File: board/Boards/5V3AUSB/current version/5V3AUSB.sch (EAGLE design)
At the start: 11 parts

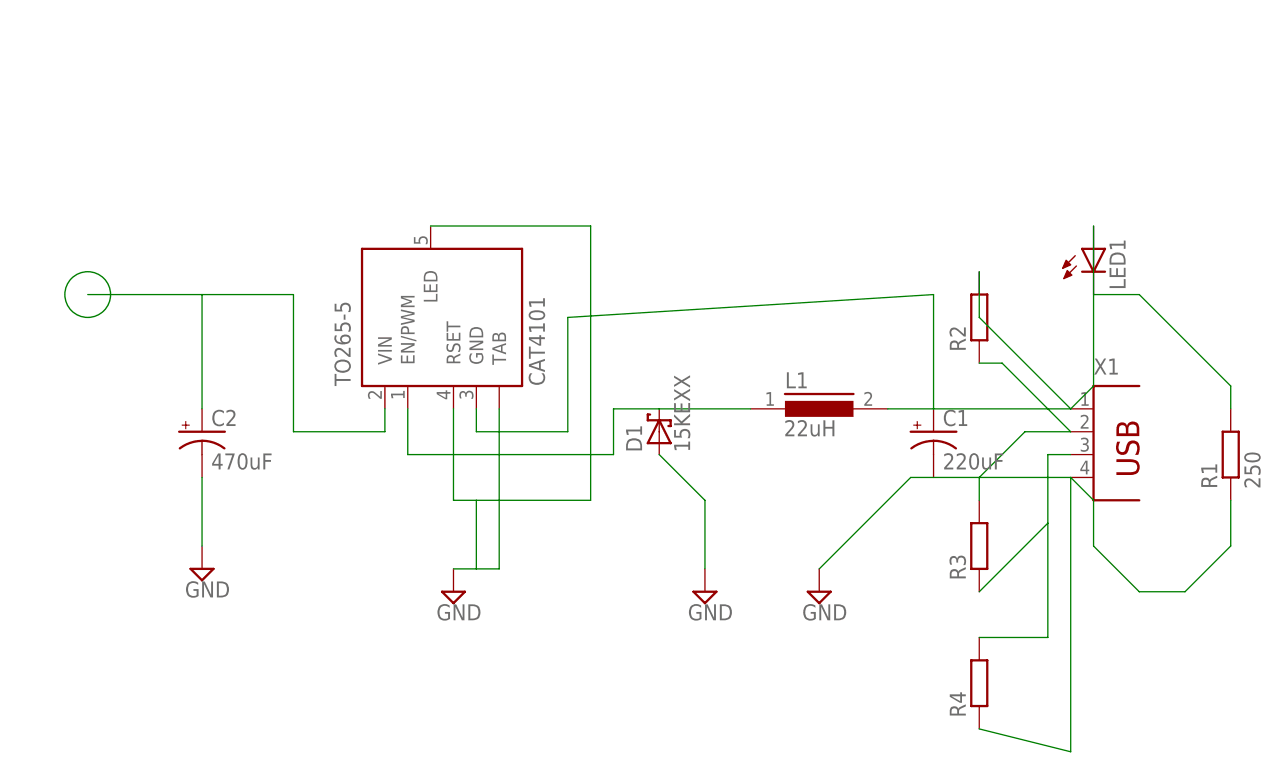
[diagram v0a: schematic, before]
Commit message: updates to the 5V3A board
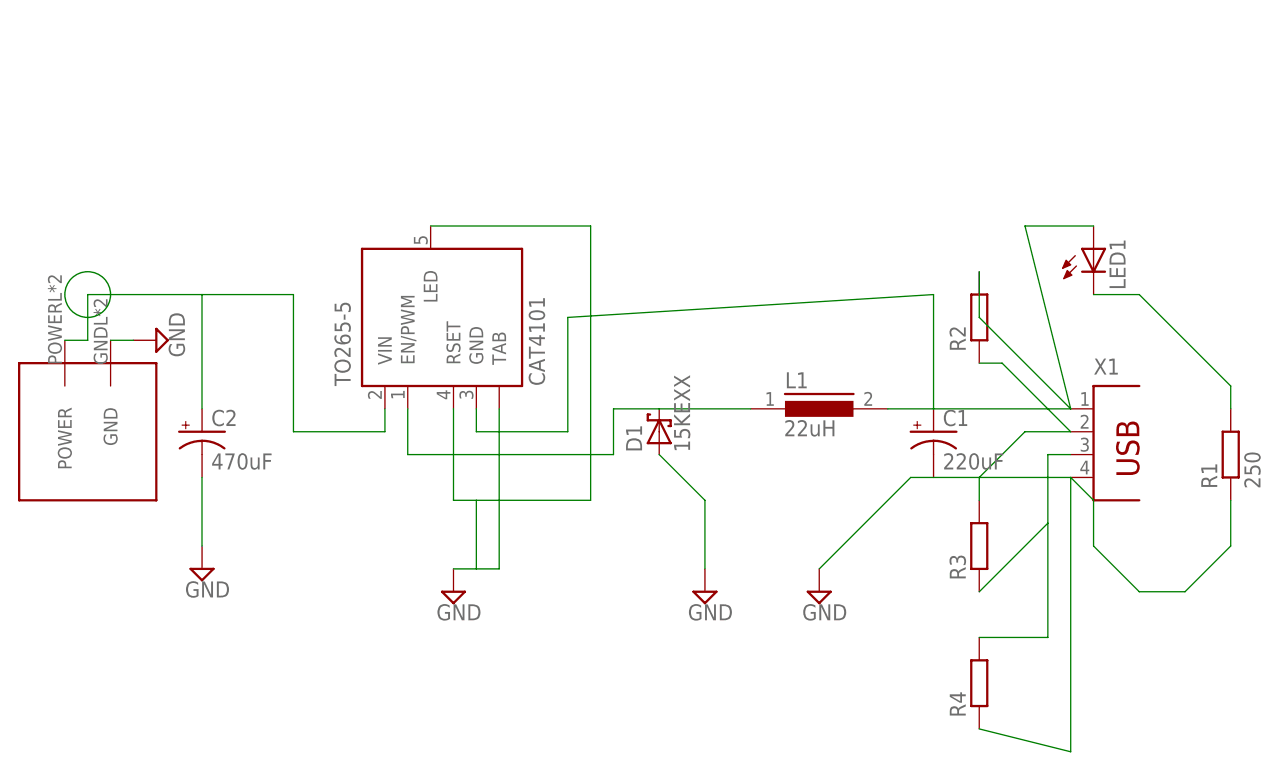
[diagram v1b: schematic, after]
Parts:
- added U$1: 2X2-MOLEX, Molex:2X2-MOLEX
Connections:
- net GND: now also U$1.GND
- net N$1: now also U$1.POWER
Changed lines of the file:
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@@
 <part name="LED1" library="led" deviceset="LED" device="CHIPLED_1206"/>
 <part name="R1" library="resistor" deviceset="R-EU_" device="R1206" value="250"/>
+<part name="U$1" library="Molex" deviceset="2X2-MOLEX" device=""/>
+<part name="SUPPLY5" library="supply2" deviceset="GND" device=""/>
 </parts>
 <sheets>
@@
 <instance part="LED1" gate="G$1" x="137.16" y="121.92"/>
 <instance part="R1" gate="G$1" x="152.4" y="99.06" rot="R90"/>
+<instance part="U$1" gate="G$1" x="25.4" y="99.06"/>
+<instance part="SUPPLY5" gate="GND" x="33.02" y="111.76" rot="R90"/>
 </instances>
 <busses>
@@
 <pinref part="TO265-5" gate="G$1" pin="VIN"/>
 <wire x1="58.42" y1="101.6" x2="58.42" y2="104.14" width="0.1524" layer="91"/>
+<pinref part="U$1" gate="G$1" pin="POWER"/>
+<wire x1="22.86" y1="111.76" x2="25.4" y2="111.76" width="0.1524" layer="91"/>
+<wire x1="25.4" y1="111.76" x2="25.4" y2="116.84" width="0.1524" layer="91"/>
 </segment>
 </net>
@@
 <wire x1="68.58" y1="86.36" x2="71.12" y2="86.36" width="0.1524" layer="91"/>
 </segment>
+<segment>
+<pinref part="U$1" gate="G$1" pin="GND"/>
+<pinref part="SUPPLY5" gate="GND" pin="GND"/>
+<wire x1="27.94" y1="111.76" x2="30.48" y2="111.76" width="0.1524" layer="91"/>
+</segment>
 </net>
 <net name="N$2" class="0">
@@
 <wire x1="119.38" y1="104.14" x2="134.62" y2="104.14" width="0.1524" layer="91"/>
 <pinref part="LED1" gate="G$1" pin="A"/>
-<wire x1="137.16" y1="124.46" x2="137.16" y2="106.68" width="0.1524" layer="91"/>
-<wire x1="137.16" y1="106.68" x2="134.62" y2="104.14" width="0.1524" layer="91"/>
+<wire x1="137.16" y1="124.46" x2="129.54" y2="124.46" width="0.1524" layer="91"/>
+<wire x1="129.54" y1="124.46" x2="134.62" y2="104.14" width="0.1524" layer="91"/>
 </segment>
 </net>

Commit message: getting ready to add pads out +5V
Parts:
- added TP1, TP2: TP2P2-38-20, testpad:TP2P2-38-20
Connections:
- net GND: now also TP1B.TP, TP2B.TP
- net N$3: now also TP1A.TP, TP2A.TP
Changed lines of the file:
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@@
 <part name="U$1" library="Molex" deviceset="2X2-MOLEX" device=""/>
 <part name="SUPPLY5" library="supply2" deviceset="GND" device=""/>
+<part name="TP1" library="testpad" deviceset="TP2" device="P2-38-20"/>
+<part name="TP2" library="testpad" deviceset="TP2" device="P2-38-20"/>
+<part name="SUPPLY6" library="supply2" deviceset="GND" device=""/>
 </parts>
 <sheets>
@@
 <instance part="U$1" gate="G$1" x="25.4" y="99.06"/>
 <instance part="SUPPLY5" gate="GND" x="33.02" y="111.76" rot="R90"/>
+<instance part="TP1" gate="A" x="86.36" y="127"/>
+<instance part="TP1" gate="B" x="93.98" y="127"/>
+<instance part="TP2" gate="A" x="101.6" y="127"/>
+<instance part="TP2" gate="B" x="109.22" y="127"/>
+<instance part="SUPPLY6" gate="GND" x="116.84" y="121.92"/>
 </instances>
 <busses>
@@
 <wire x1="27.94" y1="111.76" x2="30.48" y2="111.76" width="0.1524" layer="91"/>
 </segment>
+<segment>
+<pinref part="TP1" gate="B" pin="TP"/>
+<wire x1="93.98" y1="124.46" x2="96.52" y2="124.46" width="0.1524" layer="91"/>
+<wire x1="96.52" y1="124.46" x2="96.52" y2="129.54" width="0.1524" layer="91"/>
+<pinref part="SUPPLY6" gate="GND" pin="GND"/>
+<wire x1="96.52" y1="129.54" x2="116.84" y2="129.54" width="0.1524" layer="91"/>
+<wire x1="116.84" y1="129.54" x2="116.84" y2="124.46" width="0.1524" layer="91"/>
+<pinref part="TP2" gate="B" pin="TP"/>
+<wire x1="109.22" y1="124.46" x2="111.76" y2="124.46" width="0.1524" layer="91"/>
+<wire x1="111.76" y1="124.46" x2="111.76" y2="127" width="0.1524" layer="91"/>
+<wire x1="111.76" y1="127" x2="114.3" y2="127" width="0.1524" layer="91"/>
+<wire x1="114.3" y1="127" x2="114.3" y2="124.46" width="0.1524" layer="91"/>
+<wire x1="114.3" y1="124.46" x2="116.84" y2="124.46" width="0.1524" layer="91"/>
+</segment>
 </net>
 <net name="N$2" class="0">
@@
 <wire x1="137.16" y1="124.46" x2="129.54" y2="124.46" width="0.1524" layer="91"/>
 <wire x1="129.54" y1="124.46" x2="134.62" y2="104.14" width="0.1524" layer="91"/>
+<pinref part="TP1" gate="A" pin="TP"/>
+<wire x1="86.36" y1="124.46" x2="119.38" y2="104.14" width="0.1524" layer="91"/>
+<pinref part="TP2" gate="A" pin="TP"/>
+<wire x1="101.6" y1="124.46" x2="119.38" y2="104.14" width="0.1524" layer="91"/>
 </segment>
 </net>

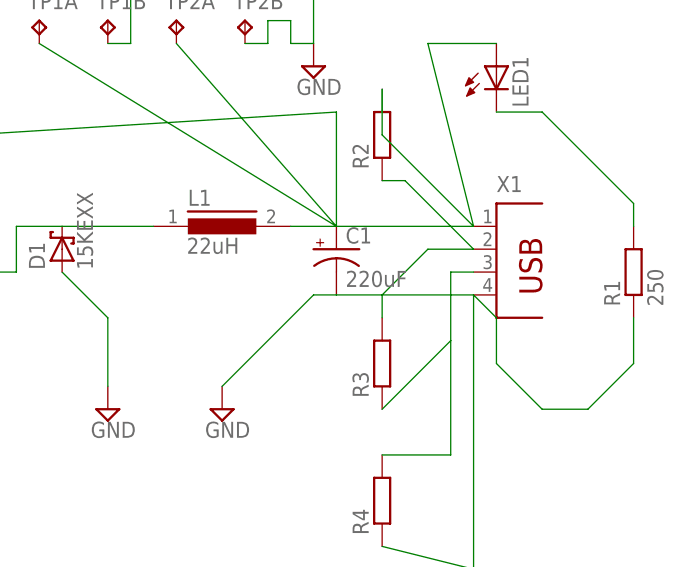
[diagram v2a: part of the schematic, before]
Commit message: board placement is looking good. going to verify schematic now
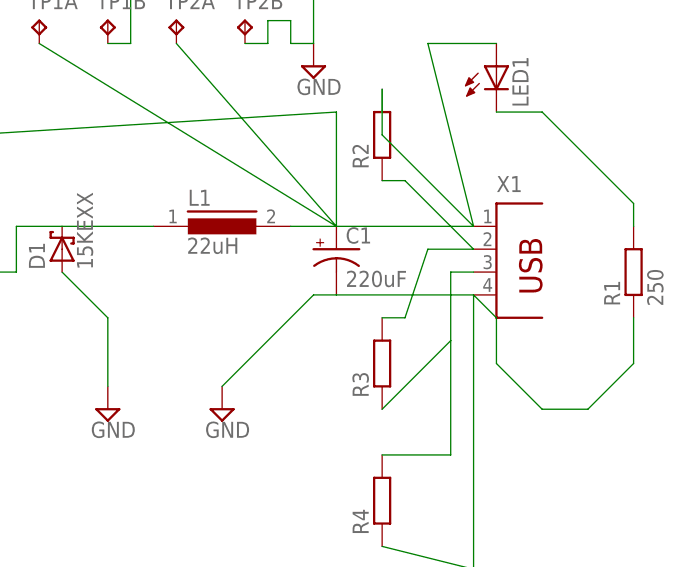
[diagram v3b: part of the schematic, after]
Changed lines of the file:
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@@
 <segment>
 <pinref part="R3" gate="G$1" pin="2"/>
-<wire x1="124.46" y1="93.98" x2="124.46" y2="96.52" width="0.1524" layer="91"/>
-<wire x1="124.46" y1="96.52" x2="129.54" y2="101.6" width="0.1524" layer="91"/>
+<wire x1="124.46" y1="93.98" x2="127" y2="93.98" width="0.1524" layer="91"/>
+<wire x1="127" y1="93.98" x2="129.54" y2="101.6" width="0.1524" layer="91"/>
 <pinref part="X1" gate="G$1" pin="2"/>
 <wire x1="129.54" y1="101.6" x2="134.62" y2="101.6" width="0.1524" layer="91"/>

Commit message: everything reworked except the power out
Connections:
- net GND: now also TO265-5.GND; no longer TO265-5.RSET
- net N$1: now also TO265-5.EN/PWM; no longer TO265-5.VIN
- net N$2: now also TO265-5.VIN; no longer TO265-5.EN/PWM
- net N$3: now also TO265-5.RSET; no longer TO265-5.GND
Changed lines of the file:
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@@
 <wire x1="38.1" y1="116.84" x2="48.26" y2="116.84" width="0.1524" layer="91"/>
 <wire x1="48.26" y1="116.84" x2="48.26" y2="101.6" width="0.1524" layer="91"/>
-<wire x1="48.26" y1="101.6" x2="58.42" y2="101.6" width="0.1524" layer="91"/>
-<pinref part="TO265-5" gate="G$1" pin="VIN"/>
-<wire x1="58.42" y1="101.6" x2="58.42" y2="104.14" width="0.1524" layer="91"/>
 <pinref part="U$1" gate="G$1" pin="POWER"/>
 <wire x1="22.86" y1="111.76" x2="25.4" y2="111.76" width="0.1524" layer="91"/>
 <wire x1="25.4" y1="111.76" x2="25.4" y2="116.84" width="0.1524" layer="91"/>
+<pinref part="TO265-5" gate="G$1" pin="EN/PWM"/>
+<wire x1="48.26" y1="101.6" x2="60.96" y2="101.6" width="0.1524" layer="91"/>
+<wire x1="60.96" y1="101.6" x2="60.96" y2="104.14" width="0.1524" layer="91"/>
 </segment>
 </net>
@@
 <wire x1="81.28" y1="124.46" x2="81.28" y2="93.98" width="0.1524" layer="91"/>
 <wire x1="81.28" y1="93.98" x2="68.58" y2="93.98" width="0.1524" layer="91"/>
-<pinref part="TO265-5" gate="G$1" pin="RSET"/>
-<wire x1="66.04" y1="104.14" x2="66.04" y2="93.98" width="0.1524" layer="91"/>
-<wire x1="66.04" y1="93.98" x2="68.58" y2="93.98" width="0.1524" layer="91"/>
 <pinref part="TO265-5" gate="G$1" pin="TAB"/>
 <wire x1="71.12" y1="104.14" x2="71.12" y2="86.36" width="0.1524" layer="91"/>
 <wire x1="68.58" y1="86.36" x2="71.12" y2="86.36" width="0.1524" layer="91"/>
+<pinref part="TO265-5" gate="G$1" pin="GND"/>
+<wire x1="68.58" y1="104.14" x2="68.58" y2="93.98" width="0.1524" layer="91"/>
 </segment>
 <segment>
@@
 <pinref part="L1" gate="1" pin="1"/>
 <wire x1="88.9" y1="104.14" x2="99.06" y2="104.14" width="0.1524" layer="91"/>
-<pinref part="TO265-5" gate="G$1" pin="EN/PWM"/>
-<wire x1="60.96" y1="104.14" x2="60.96" y2="99.06" width="0.1524" layer="91"/>
-<wire x1="60.96" y1="99.06" x2="83.82" y2="99.06" width="0.1524" layer="91"/>
+<wire x1="58.42" y1="99.06" x2="83.82" y2="99.06" width="0.1524" layer="91"/>
 <wire x1="83.82" y1="99.06" x2="83.82" y2="104.14" width="0.1524" layer="91"/>
 <wire x1="83.82" y1="104.14" x2="88.9" y2="104.14" width="0.1524" layer="91"/>
+<pinref part="TO265-5" gate="G$1" pin="VIN"/>
+<wire x1="58.42" y1="99.06" x2="58.42" y2="104.14" width="0.1524" layer="91"/>
 </segment>
 </net>
@@
 <pinref part="C1" gate="G$1" pin="+"/>
 <wire x1="114.3" y1="104.14" x2="119.38" y2="104.14" width="0.1524" layer="91"/>
-<pinref part="TO265-5" gate="G$1" pin="GND"/>
-<wire x1="68.58" y1="104.14" x2="68.58" y2="101.6" width="0.1524" layer="91"/>
-<wire x1="68.58" y1="101.6" x2="78.74" y2="101.6" width="0.1524" layer="91"/>
-<wire x1="78.74" y1="101.6" x2="78.74" y2="114.3" width="0.1524" layer="91"/>
 <wire x1="78.74" y1="114.3" x2="119.38" y2="116.84" width="0.1524" layer="91"/>
 <wire x1="119.38" y1="116.84" x2="119.38" y2="104.14" width="0.1524" layer="91"/>
@@
 <pinref part="TP2" gate="A" pin="TP"/>
 <wire x1="101.6" y1="124.46" x2="119.38" y2="104.14" width="0.1524" layer="91"/>
+<wire x1="78.74" y1="114.3" x2="78.74" y2="101.6" width="0.1524" layer="91"/>
+<pinref part="TO265-5" gate="G$1" pin="RSET"/>
+<wire x1="78.74" y1="101.6" x2="66.04" y2="101.6" width="0.1524" layer="91"/>
+<wire x1="66.04" y1="101.6" x2="66.04" y2="104.14" width="0.1524" layer="91"/>
 </segment>
 </net>

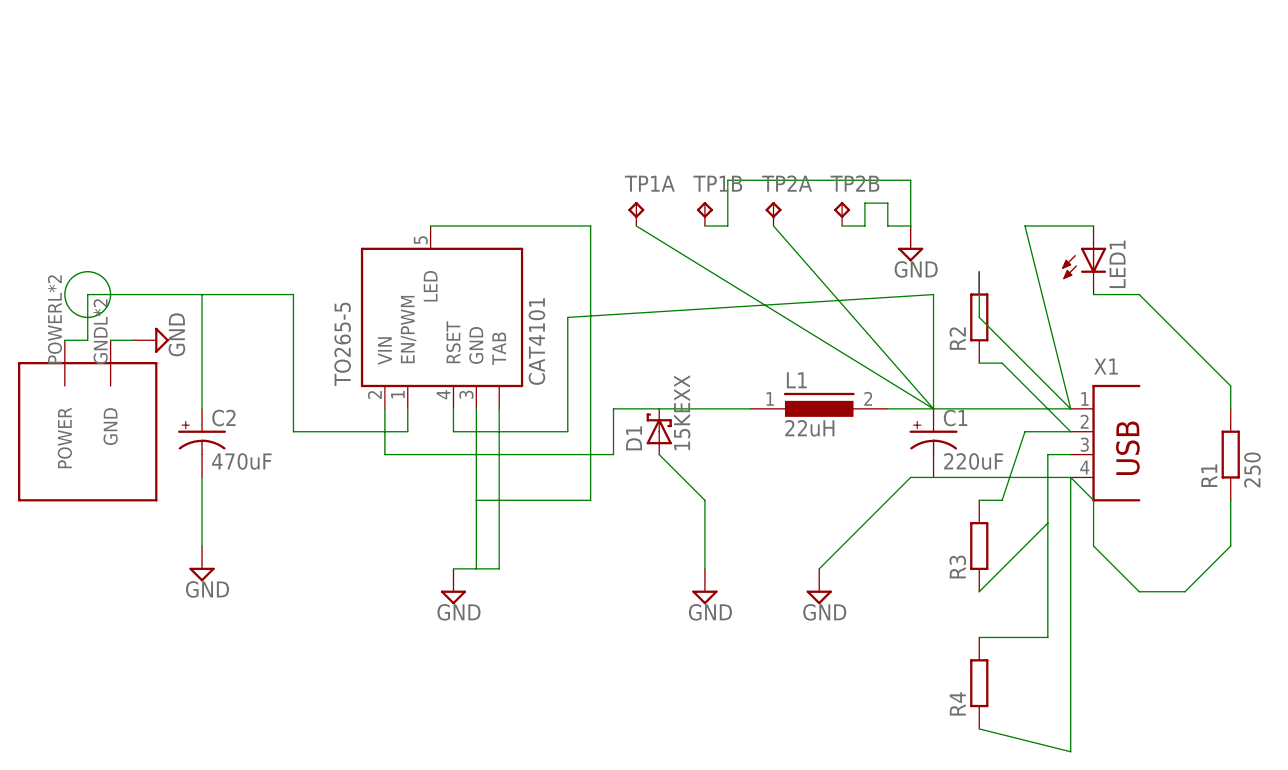
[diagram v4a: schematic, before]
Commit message: added new board, complete revision of everything
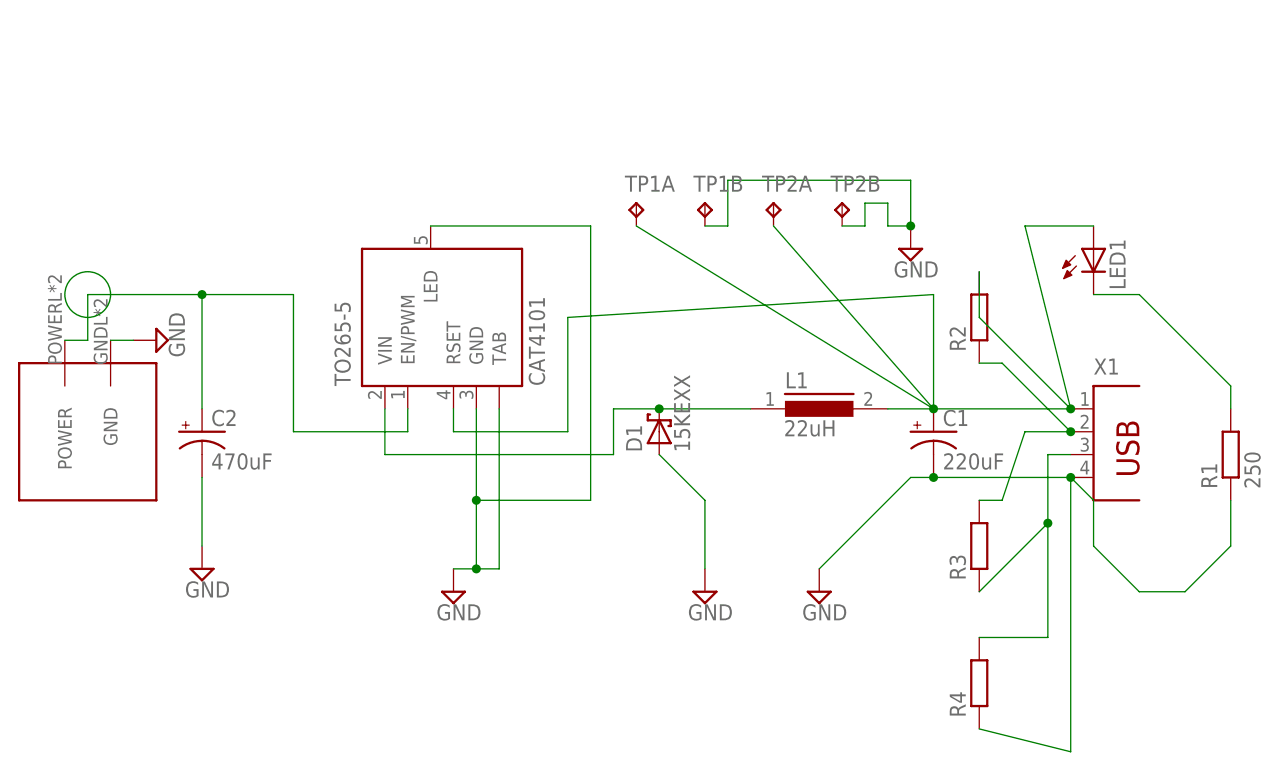
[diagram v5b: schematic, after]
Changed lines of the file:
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@@
 <wire x1="48.26" y1="101.6" x2="60.96" y2="101.6" width="0.1524" layer="91"/>
 <wire x1="60.96" y1="101.6" x2="60.96" y2="104.14" width="0.1524" layer="91"/>
+<junction x="38.1" y="116.84"/>
 </segment>
 </net>
@@
 <pinref part="R1" gate="G$1" pin="1"/>
 <wire x1="152.4" y1="93.98" x2="152.4" y2="88.9" width="0.1524" layer="91"/>
+<junction x="119.38" y="96.52"/>
+<junction x="134.62" y="96.52"/>
 </segment>
 <segment>
@@
 <pinref part="TO265-5" gate="G$1" pin="GND"/>
 <wire x1="68.58" y1="104.14" x2="68.58" y2="93.98" width="0.1524" layer="91"/>
+<junction x="68.58" y="93.98"/>
+<junction x="68.58" y="86.36"/>
 </segment>
 <segment>
@@
 <wire x1="114.3" y1="127" x2="114.3" y2="124.46" width="0.1524" layer="91"/>
 <wire x1="114.3" y1="124.46" x2="116.84" y2="124.46" width="0.1524" layer="91"/>
+<junction x="116.84" y="124.46"/>
 </segment>
 </net>
@@
 <pinref part="TO265-5" gate="G$1" pin="VIN"/>
 <wire x1="58.42" y1="99.06" x2="58.42" y2="104.14" width="0.1524" layer="91"/>
+<junction x="88.9" y="104.14"/>
 </segment>
 </net>
@@
 <wire x1="78.74" y1="101.6" x2="66.04" y2="101.6" width="0.1524" layer="91"/>
 <wire x1="66.04" y1="101.6" x2="66.04" y2="104.14" width="0.1524" layer="91"/>
+<junction x="119.38" y="104.14"/>
+<junction x="134.62" y="104.14"/>
 </segment>
 </net>
@@
 <wire x1="132.08" y1="99.06" x2="132.08" y2="91.44" width="0.1524" layer="91"/>
 <wire x1="132.08" y1="91.44" x2="124.46" y2="83.82" width="0.1524" layer="91"/>
+<junction x="132.08" y="91.44"/>
 </segment>
 </net>
@@
 <wire x1="124.46" y1="109.22" x2="127" y2="109.22" width="0.1524" layer="91"/>
 <wire x1="127" y1="109.22" x2="134.62" y2="101.6" width="0.1524" layer="91"/>
+<junction x="134.62" y="101.6"/>
 </segment>
 </net>
